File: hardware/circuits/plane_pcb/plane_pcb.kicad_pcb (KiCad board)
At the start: 2 copper layers, 32 parts, among them J1 J1, J2 J2, J3 J3, J4 J4, U1 Magnetometer_Breakout, U2 U1

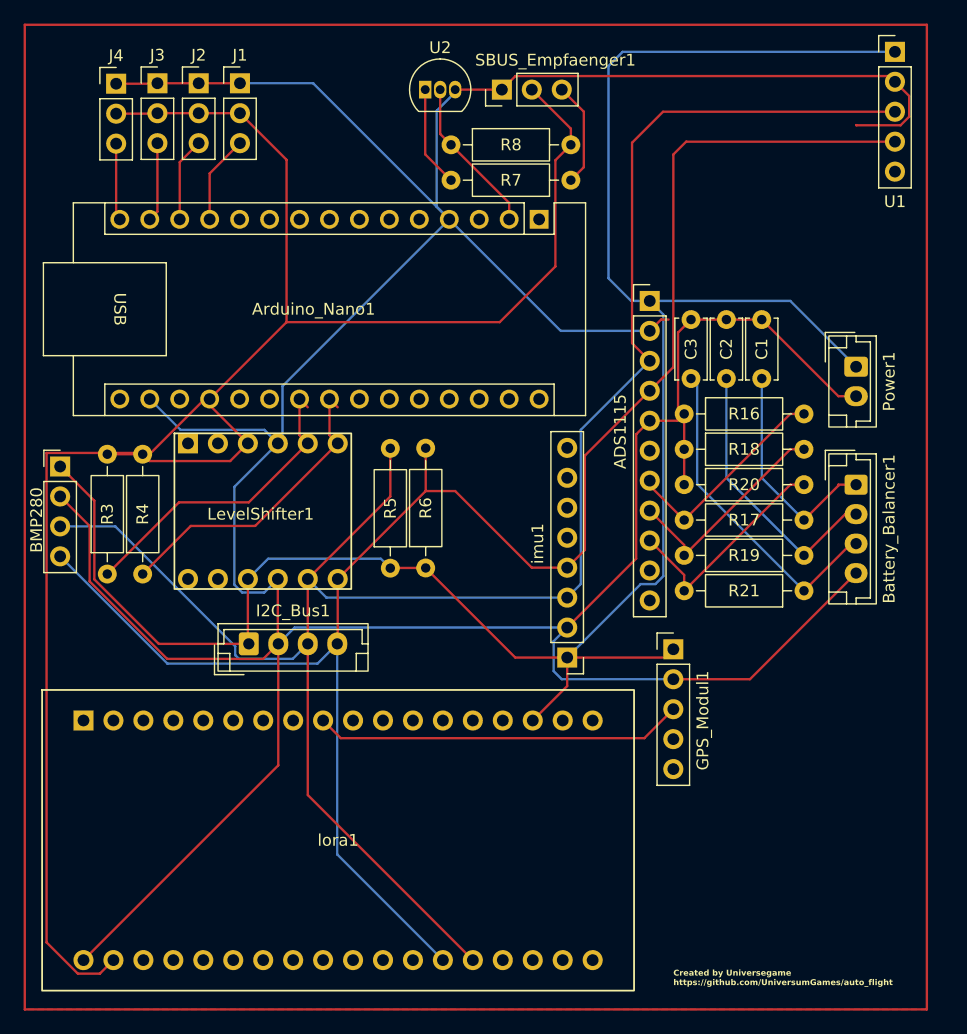
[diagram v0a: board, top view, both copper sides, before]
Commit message: update to smd components
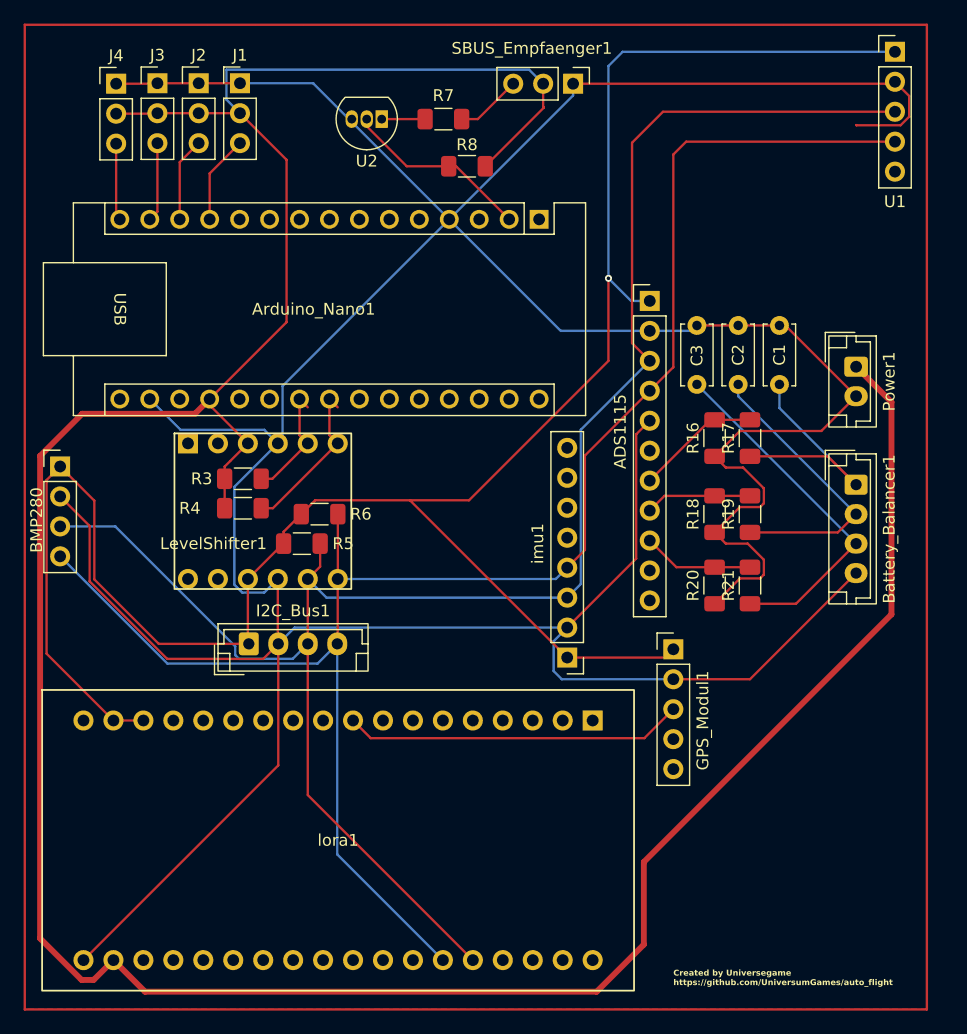
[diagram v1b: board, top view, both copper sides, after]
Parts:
- R16, R17, R18, R19, R20, R21, R3, R4, R5, R6, R7, R8: footprint Resistor_THT:R_Axial_DIN0207_L6.3mm_D2.5mm_P10.16mm_Horizontal -> Resistor_SMD:R_1206_3216Metric_Pad1.30x1.75mm_HandSolder
- moved R3 14.1 mm to (182.0, 108.0), turned to 180 degrees
- moved R7 12.0 mm to (199.0, 77.5)
- moved R4 10.2 mm to (182.0, 110.5), turned to 180 degrees
- moved R6 10.1 mm to (188.5, 111.0), turned to 0 degrees
- moved R20 8.93 mm to (222.0, 117.0), turned to 90 degrees
- moved R17 8.32 mm to (225.0, 104.5), turned to 90 degrees
- moved R5 7.78 mm to (187.0, 113.5), turned to 0 degrees
- moved R18 6.08 mm to (222.0, 111.0), turned to 90 degrees
- moved SBUS_Empfaenger1 6.06 mm to (210.0, 74.5), turned to -90 degrees
- moved R19 5.76 mm to (225.0, 111.0), turned to 90 degrees
- moved R21 4.60 mm to (225.0, 117.0), turned to 90 degrees
- moved U2 4.46 mm to (193.8, 77.5), turned to 180 degrees
- moved R16 3.30 mm to (222.0, 104.5), turned to 90 degrees
- moved R8 2.27 mm to (201.0, 81.5)
- moved C1 1.58 mm to (227.5, 100.0)
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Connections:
- Power1 pad 1: /3V3 -> /5V
- lora1 pad 17: unconnected-(lora1-3V3-Pad17) -> /3V3
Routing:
- net /5V: track 163.2 -> 264.1 mm
- net Net-(Arduino_Nano1-A5): track 26.6 -> 10.2 mm
- net /GND_MAIN: track 351.2 -> 365.5 mm
- net Net-(Arduino_Nano1-A4): track 26.2 -> 13.8 mm
- net /SCL: track 167.2 -> 156.6 mm
- net Net-(ADS1115-A2): track 19.4 -> 9.44 mm
- net Net-(ADS1115-A1): track 18.9 -> 9.02 mm
- net Net-(ADS1115-A0): track 18.4 -> 10.6 mm
- net Net-(U2-B): track 8.59 -> 3.68 mm
- net /SDA: track 151.6 -> 148.1 mm
- net Net-(SBUS_Empfaenger1-Pin_3): track 8.91 -> 5.61 mm
- net /GPS_TX: track 31.3 -> 28.8 mm
- net /UART_RX: track 13.4 -> 16.0 mm
- net Net-(Battery_Balancer1-Pin_3): track 28.0 -> 30.2 mm
- net Net-(Battery_Balancer1-Pin_1): track 19.2 -> 21.2 mm
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
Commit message: finish pcb rework with smd components
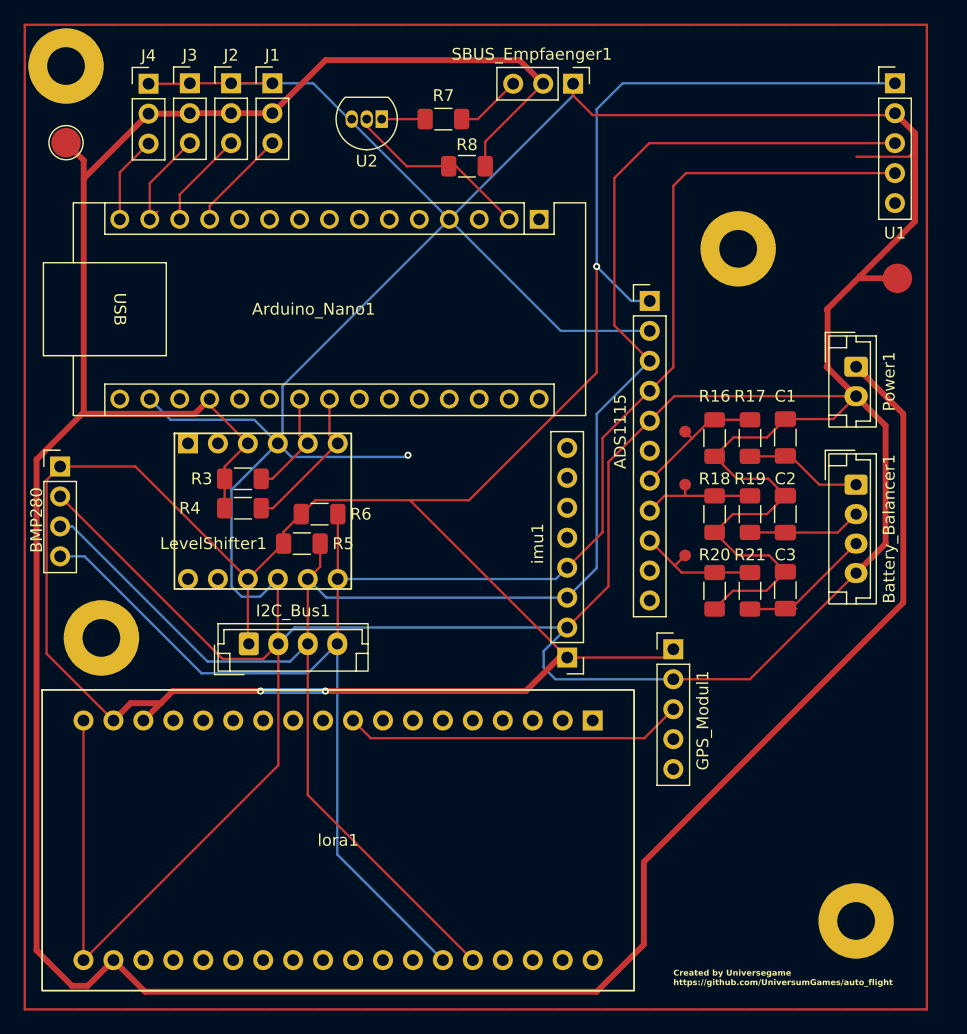
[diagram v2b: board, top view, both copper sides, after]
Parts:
- added ?: , , F.Cu at (237.5, 91.0)
- added ?: , , F.Cu at (219.5, 104.0)
- added ?: , , F.Cu at (219.5, 108.5)
- added ?: , , F.Cu at (219.5, 114.5)
- added REF**: MountingHole_3.2mm_M3_Pad, MountingHole:MountingHole_3.2mm_M3_Pad, F.Cu at (170.0, 121.5)
- added REF**: MountingHole_3.2mm_M3_Pad, MountingHole:MountingHole_3.2mm_M3_Pad, F.Cu at (167.0, 73.0)
- added REF**: TestPoint_Pad_D2.5mm, TestPoint:TestPoint_Pad_D2.5mm, F.Cu at (167.0, 79.5)
- added REF**: MountingHole_3.2mm_M3_Pad, MountingHole:MountingHole_3.2mm_M3_Pad, F.Cu at (234.0, 145.5)
- added REF**: MountingHole_3.2mm_M3_Pad, MountingHole:MountingHole_3.2mm_M3_Pad, F.Cu at (224.0, 88.5)
- C1, C2, C3: footprint Capacitor_THT:C_Disc_D5.0mm_W2.5mm_P5.00mm -> Capacitor_SMD:C_1206_3216Metric_Pad1.33x1.80mm_HandSolder
- moved C3 19.0 mm to (228.0, 117.5)
- moved C2 11.7 mm to (228.0, 111.0)
- moved C1 4.53 mm to (228.0, 104.5)
- moved J1 2.75 mm to (184.5, 74.5)
- moved J2 2.75 mm to (181.0, 74.5)
- moved J3 2.75 mm to (177.5, 74.5)
- moved J4 2.75 mm to (174.0, 74.5)
- moved U1 2.66 mm to (237.3, 74.5)
- moved R20 0.45 mm to (222.0, 117.5)
- moved R21 0.45 mm to (225.0, 117.5)
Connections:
- lora1 pad 18: unconnected-(lora1-GND-Pad18) -> /GND_MAIN
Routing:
- net /GND_MAIN: track 365.5 -> 449.9 mm, vias 0 -> 1
- net /3V3: track 180.0 -> 212.7 mm, vias 1 -> 3
- net Net-(Battery_Balancer1-Pin_3): track 30.2 -> 12.2 mm
- net Net-(Battery_Balancer1-Pin_2): track 24.8 -> 9.65 mm
- net Net-(Battery_Balancer1-Pin_1): track 21.2 -> 10.0 mm
- net /SERVO3_SIGNAL: track 6.73 -> 8.79 mm
- net /SDA: track 148.1 -> 146.1 mm
- net Net-(ADS1115-A2): track 9.44 -> 10.9 mm
- net /SERVO4_SIGNAL: track 6.55 -> 7.87 mm
- net /SERVO1_SIGNAL: track 7.52 -> 8.66 mm
- net /SERVO2_SIGNAL: track 7.13 -> 8.27 mm
- net /SCL: track 156.6 -> 155.6 mm
- net Net-(Arduino_Nano1-A5): track 10.2 -> 9.24 mm
- net Net-(Arduino_Nano1-A4): track 13.8 -> 12.8 mm
- net Net-(ADS1115-A1): track 9.02 -> 9.97 mm
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
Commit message: fix pcb issues
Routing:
- net /GND_MAIN: track 449.9 -> 427.8 mm, vias 1 -> 0
- net /SCL: track 155.6 -> 149.9 mm
- net /SDA: track 146.1 -> 150.3 mm
- net /3V3: track 212.7 -> 213.2 mm, vias 3 -> 0
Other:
- board text added: "- + Power"
- board text added: "- Battery Balancer"
- board text added: "3.3 GND SCL SDA"
- board text added: "5V"
- board text added: "Cell_1"
- board text added: "Cell_2"
- board text added: "Cell_3"
- board text added: "GND"
- board text added: "Rev1.0 (02.10.26)"

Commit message: add more pcb descriptions
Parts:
- added REF**: MountingHole_3.2mm_M3_Pad, MountingHole:MountingHole_3.2mm_M3_Pad, F.Cu at (227.0, 137.0)
- added REF**: MountingHole_3.2mm_M3_Pad, MountingHole:MountingHole_3.2mm_M3_Pad, F.Cu at (232.0, 137.0)
- added REF**: MountingHole_3.2mm_M3_Pad, MountingHole:MountingHole_3.2mm_M3_Pad, F.Cu at (232.0, 132.0)
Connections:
- REF** pad 1: (no net) -> /GND_MAIN (x4)
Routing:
- net /GND_MAIN: track 427.8 -> 454.7 mm
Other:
- board text added: "Created by Universegame https://github.com/Universumgames/auto_flight"
- board text added: "PWM"
- board text added: "S1"
- board text added: "S2"
- board text added: "S3"
- board text added: "S4"
- board text added: "Serial"
- board text removed: "Created by Universegame https://github.com/UniversumGames/auto_flight"

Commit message: fix pcb and arduino nano pinout
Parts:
- added G***: LOGO, LOGO, B.Cu at (225.5, 77.5)
- Arduino_Nano1: footprint Module:Arduino_Nano -> auto_flight:Arduino_Nano
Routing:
- net /5V: track 263.2 -> 297.1 mm
- net /SDA: track 150.3 -> 168.8 mm
- net /GND_MAIN: track 454.7 -> 441.7 mm
- net Net-(Arduino_Nano1-A5): track 9.24 -> 11.1 mm
- net unconnected-(Arduino_Nano1-3V3-Pad29): track 0.00 -> 0.60 mm
- net unconnected-(Arduino_Nano1-A0-Pad27): track 0.00 -> 0.52 mm
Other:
- board text added: "Created by Universegame https://github.com/ Universumgames/auto_flight"
- board text added: "Rev1.1 (03.10.26)"
- board text removed: "Rev1.0 (02.10.26)"

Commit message: add missing 3d models
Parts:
- ADS1115: footprint Connector_PinHeader_2.54mm:PinHeader_1x11_P2.54mm_Vertical -> Connector_PinHeader_2.54mm:PinHeader_1x10_P2.54mm_Vertical
- moved U1 7.58 mm to (237.3, 82.0), turned to 180 degrees
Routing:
- net /3V3: track 213.2 -> 197.0 mm
- net /SDA: track 168.8 -> 177.0 mm
- net /SCL: track 149.9 -> 157.0 mm
- net /GND_MAIN: track 441.7 -> 445.8 mm
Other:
- board text added: "Rev1.0_2 (04.10.26)"

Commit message: fix last pcb mistakes (hopefully) Rev1.0_2
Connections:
- lora1 pad 1: unconnected-(lora1-GPIO7-Pad1) -> /GND_MAIN
- lora1 pad 10: unconnected-(lora1-GPIO40-Pad10) -> /GPS_TX
- lora1 pad 16: /3V3 -> unconnected-(lora1-GPIO5-Pad16)
- lora1 pad 17: /3V3 -> unconnected-(lora1-GPIO6-Pad17)
- lora1 pad 18: /GND_MAIN -> unconnected-(lora1-GPIO7-Pad18)
- lora1 pad 2: unconnected-(lora1-GPIO6-Pad2) -> /3V3
- lora1 pad 3: unconnected-(lora1-GPIO5-Pad3) -> /3V3
- lora1 pad 9: /GPS_TX -> unconnected-(lora1-GPIO40-Pad9)
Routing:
- net /GND_MAIN: track 445.8 -> 457.9 mm
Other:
- board outline added: 76.5 x 83.5 mm

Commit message: fix battery percentage measurement
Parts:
- R16, R18, R20: value 33k -> 47k
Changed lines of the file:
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@@
 			)
 		)
-		(property "Value" "33k"
+		(property "Value" "47k"
 			(at 0 1.83 90)
 			(layer "F.Fab")
@@
 			)
 		)
-		(property "Value" "33k"
+		(property "Value" "47k"
 			(at 0 1.83 90)
 			(layer "F.Fab")
@@
 			)
 		)
-		(property "Value" "33k"
+		(property "Value" "47k"
 			(at 0 1.83 90)
 			(layer "F.Fab")
